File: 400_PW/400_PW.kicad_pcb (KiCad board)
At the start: 2 copper layers, 97.4 x 67.5 mm, 0 parts

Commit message: Update schematics
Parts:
- added C1: C_0038, DVB_Capacitors_Ceramic:C_1206, F.Cu at (131.7, 262.0)
- added C10: C_0032, DVB_Capacitors_Ceramic:C_0805, F.Cu at (147.6, 250.1)
- added C11: C_0002, DVB_Capacitors_Ceramic:C_0402, F.Cu at (102.6, 268.9)
- added C12: C_0002, DVB_Capacitors_Ceramic:C_0402, F.Cu at (121.7, 263.1)
- added C13: C_0002, DVB_Capacitors_Ceramic:C_0402, F.Cu at (141.5, 258.9)
- added C14: C_0038, DVB_Capacitors_Ceramic:C_1206, F.Cu at (142.1, 246.2)
- added C15: C_0037, DVB_Capacitors_Ceramic:C_0603, F.Cu at (157.9, 241.4)
- added C16: C_0037, DVB_Capacitors_Ceramic:C_0603, F.Cu at (152.4, 246.1)
- added C17: C_0037, DVB_Capacitors_Ceramic:C_0603, F.Cu at (141.9, 256.7)
- added C18: C_0032, DVB_Capacitors_Ceramic:C_0805, F.Cu at (136.8, 261.8)
- added C19: C_0071, DVB_Capacitors_Ceramic:C_2220, F.Cu at (117.6, 254.3)
- added C2: C_0038, DVB_Capacitors_Ceramic:C_1206, F.Cu at (131.6, 253.7)
- added C20: C_0012, DVB_Capacitors_Ceramic:C_0603, F.Cu at (110.6, 235.3)
- added C21: C_0012, DVB_Capacitors_Ceramic:C_0603, F.Cu at (157.9, 239.1)
- added C22: C_0012, DVB_Capacitors_Ceramic:C_0603, F.Cu at (118.0, 241.3)
- added C23: C_0071, DVB_Capacitors_Ceramic:C_2220, F.Cu at (139.0, 231.4)
- added C24: C_0039, DVB_Capacitors_Ceramic:C_0402, F.Cu at (114.1, 235.1)
- added C25: C_0039, DVB_Capacitors_Ceramic:C_0402, F.Cu at (140.6, 261.4)
- added C26: C_0039, DVB_Capacitors_Ceramic:C_0402, F.Cu at (102.6, 266.9)
- added C27: C_0040, DVB_Capacitors_Ceramic:C_1210, F.Cu at (149.9, 236.9)
- added C28: C_0040, DVB_Capacitors_Ceramic:C_1210, F.Cu at (131.6, 257.3)
- added C29: C_0040, DVB_Capacitors_Ceramic:C_1210, F.Cu at (147.7, 242.5)
- added C3: C_0038, DVB_Capacitors_Ceramic:C_1206, F.Cu at (98.3, 267.4)
- added C30: C_0071, DVB_Capacitors_Ceramic:C_2220, F.Cu at (108.9, 261.1)
- added C31: C_0040, DVB_Capacitors_Ceramic:C_1210, F.Cu at (155.4, 235.9)
- added C32: C_0040, DVB_Capacitors_Ceramic:C_1210, F.Cu at (126.2, 264.1)
- added C33: C_0040, DVB_Capacitors_Ceramic:C_1210, F.Cu at (137.2, 254.3)
- added C34: C_0040, DVB_Capacitors_Ceramic:C_1210, F.Cu at (147.7, 246.6)
- added C35: C_0040, DVB_Capacitors_Ceramic:C_1210, F.Cu at (126.2, 268.2)
- added C36: C_0040, DVB_Capacitors_Ceramic:C_1210, F.Cu at (163.1, 258.9)
- added C37: C_0040, DVB_Capacitors_Ceramic:C_1210, F.Cu at (137.2, 258.4)
- added C38: C_0040, DVB_Capacitors_Ceramic:C_1210, F.Cu at (138.0, 250.2)
- added C39: C_0040, DVB_Capacitors_Ceramic:C_1210, F.Cu at (120.6, 266.6)
- added C4: C_0002, DVB_Capacitors_Ceramic:C_0402, F.Cu at (127.2, 259.9)
- added C40: C_0037, DVB_Capacitors_Ceramic:C_0603, F.Cu at (163.6, 264.5)
- added C41: C_0057, DVB_Capacitors_Ceramic:C_0603, F.Cu at (163.6, 262.2)
- added C42: C_0041, DVB_Capacitors_Ceramic:C_1206, F.Cu at (153.2, 240.5)
- added C43: C_0056, DVB_Capacitors_Ceramic:C_0805, F.Cu at (131.2, 265.0)
- added C44: C_0003, DVB_Capacitors_Ceramic:C_0603, F.Cu at (121.8, 241.3)
- added C45: C_0058, DVB_Capacitors_Tantalum:CP_EIA-7343-31, F.Cu at (92.7, 237.0)
- added C5: C_0038, DVB_Capacitors_Ceramic:C_1206, F.Cu at (132.5, 249.8)
- added C6: C_0038, DVB_Capacitors_Ceramic:C_1206, F.Cu at (142.1, 243.0)
- added C7: C_0038, DVB_Capacitors_Ceramic:C_1206, F.Cu at (122.9, 260.5)
- added C8: C_0032, DVB_Capacitors_Ceramic:C_0805, F.Cu at (152.7, 243.5)
- added C9: C_0032, DVB_Capacitors_Ceramic:C_0805, F.Cu at (143.1, 250.1)
- added D1: D_0026, DVB_Diodes:D_SMA, F.Cu at (109.4, 251.0)
- added D2: D_0026, DVB_Diodes:D_SMA, F.Cu at (130.8, 230.4)
- added D3: D_0026, DVB_Diodes:D_SMA, F.Cu at (129.2, 236.4)
- added D4: D_0026, DVB_Diodes:D_SMA, F.Cu at (100.4, 263.6)
- added D5: D_0026, DVB_Diodes:D_SMA, F.Cu at (91.4, 266.3)
- added D6: D_0026, DVB_Diodes:D_SMA, F.Cu at (109.4, 255.6)
- added J1: TESTBAT-14, DVB_Connectors:Solder_Pad_8x5, B.Cu at (203.7, 207.8)
- added J10: GNDBATT-4B, DVB_Connectors:Solder_Pad_8x5, B.Cu at (203.1, 187.9)
- added J11: GND-7_21_22_3B_28_51B_53_76, DVB_Connectors:Solder_Pad_8x5, B.Cu at (204.1, 227.0)
- added J12: TESTBAT-14, DVB_Connectors:Solder_Pad_8x5, B.Cu at (203.9, 238.7)
- added J2: ON/OFF-6A, DVB_Connectors:Solder_Pad_8x5, B.Cu at (137.7, 169.4)
- added J3: +7.5V-13_26_33_51A_54_104_6A, DVB_Connectors:Solder_Pad_8x5, B.Cu at (203.5, 249.1)
- added J4: +4.9V-10_36_80_83_93, DVB_Connectors:Solder_Pad_8x5, B.Cu at (152.1, 171.5)
- added J5: -4.9V, DVB_Connectors:Solder_Pad_8x5, B.Cu at (203.4, 198.0)
- added J6: +48V, DVB_Connectors:Solder_Pad_8x5, B.Cu at (195.4, 176.2)
- added J7: BATT-4A_6B, DVB_Connectors:Solder_Pad_8x5, B.Cu at (204.0, 218.9)
- added J8: 15VIN-3A, DVB_Connectors:Solder_Pad_8x5, B.Cu at (200.3, 268.6)
- added J9: GNDAKKU-5, DVB_Connectors:Solder_Pad_8x5, B.Cu at (178.9, 171.3)
- added K1: K_0008, Connector_JST:JST_EH_B3B-EH-A_1x03_P2.50mm_Vertical, B.Cu at (87.1, 186.7)
- added L1: L_0001, DVB_Inductors:L_0805, F.Cu at (130.8, 267.8)
- added L10: L_0004, DVB_Inductors:L_2020-Vishay, F.Cu at (116.6, 261.2)
- added L11: L_0001, DVB_Inductors:L_0805, F.Cu at (151.8, 250.1)
- added L12: L_0004, DVB_Inductors:L_2020-Vishay, F.Cu at (136.9, 238.0)
- added L2: L_0001, DVB_Inductors:L_0805, F.Cu at (147.2, 252.9)
- added L3: L_0001, DVB_Inductors:L_0805, F.Cu at (135.4, 265.0)
- added L4: L_0004, DVB_Inductors:L_2020-Vishay, F.Cu at (146.7, 231.5)
- added L5: L_0004, DVB_Inductors:L_2020-Vishay, F.Cu at (135.8, 244.8)
- added L6: L_0004, DVB_Inductors:L_2020-Vishay, F.Cu at (125.3, 255.5)
- added L7: L_0015, DVB_Inductors:L_7050-Wurth, F.Cu at (104.0, 232.4)
- added L8: L_0004, DVB_Inductors:L_2020-Vishay, F.Cu at (126.1, 248.8)
- added L9: L_0004, DVB_Inductors:L_2020-Vishay, F.Cu at (128.6, 242.0)
- added R1: R_0002, DVB_Resistors:R_0402, F.Cu at (155.6, 246.0)
- added R10: R_0002, DVB_Resistors:R_0402, F.Cu at (143.4, 261.1)
- added R11: R_0155, DVB_Resistors:R_0402, F.Cu at (158.3, 245.9)
- added R12: R_0002, DVB_Resistors:R_0402, F.Cu at (147.8, 255.4)
- added R13: R_0158, DVB_Resistors:R_0402, F.Cu at (164.6, 269.0)
- added R14: R_0002, DVB_Resistors:R_0402, F.Cu at (144.3, 258.9)
- added R15: R_0008, DVB_Resistors:R_0402, F.Cu at (145.1, 256.6)
- added R16: R_0112, DVB_Resistors:R_0402, F.Cu at (155.6, 248.2)
- added R17: R_0128, DVB_Resistors:R_0402, F.Cu at (150.4, 252.6)
- added R18: R_0099, DVB_Resistors:R_1206, F.Cu at (142.6, 253.9)
- added R19: R_0157, DVB_Resistors:R_0402, F.Cu at (138.6, 264.3)
- added R2: R_0159, DVB_Resistors:R_0402, F.Cu at (156.3, 243.7)
- added R20: R_0034, DVB_Resistors:R_0402, F.Cu at (159.0, 243.7)
- added R21: R_0020, DVB_Resistors:R_0402, F.Cu at (134.0, 267.5)
- added R3: R_0156, DVB_Resistors:R_0402, F.Cu at (164.6, 266.8)
- added R4: R_0156, DVB_Resistors:R_0402, F.Cu at (136.7, 267.5)
- added R5: R_0156, DVB_Resistors:R_0402, F.Cu at (150.4, 254.8)
- added R6: R_0154, DVB_Resistors:R_0402, F.Cu at (155.0, 250.3)
- added R7: R_0118, DVB_Resistors:R_0402, F.Cu at (153.0, 252.6)
- added R8: R_0002, DVB_Resistors:R_0402, F.Cu at (147.8, 257.6)
- added R9: R_0155, DVB_Resistors:R_0402, F.Cu at (141.2, 263.6)
- added RV1: 25K, Potentiometer_THT:Potentiometer_Piher_PT-6-V_Vertical_Hole, F.Cu at (174.6, 246.6)
- added U1: U_0064, DVB_SSOP:MSOP_16-1EP_3x4_P0.5, F.Cu at (114.5, 267.5)
- added U2: U_0064, DVB_SSOP:MSOP_16-1EP_3x4_P0.5, F.Cu at (107.9, 267.3)
- added U3: U_0064, DVB_SSOP:MSOP_16-1EP_3x4_P0.5, F.Cu at (153.6, 231.0)
- added U4: U_0126, DVB_SOIC:SOIC_8, F.Cu at (100.6, 258.0)
- added U5: U_0089, DVB_SSOP:MSOP_12-1EP_3x4_P0.65, F.Cu at (143.8, 237.7)
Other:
- outline, holes or cut-outs redrawn

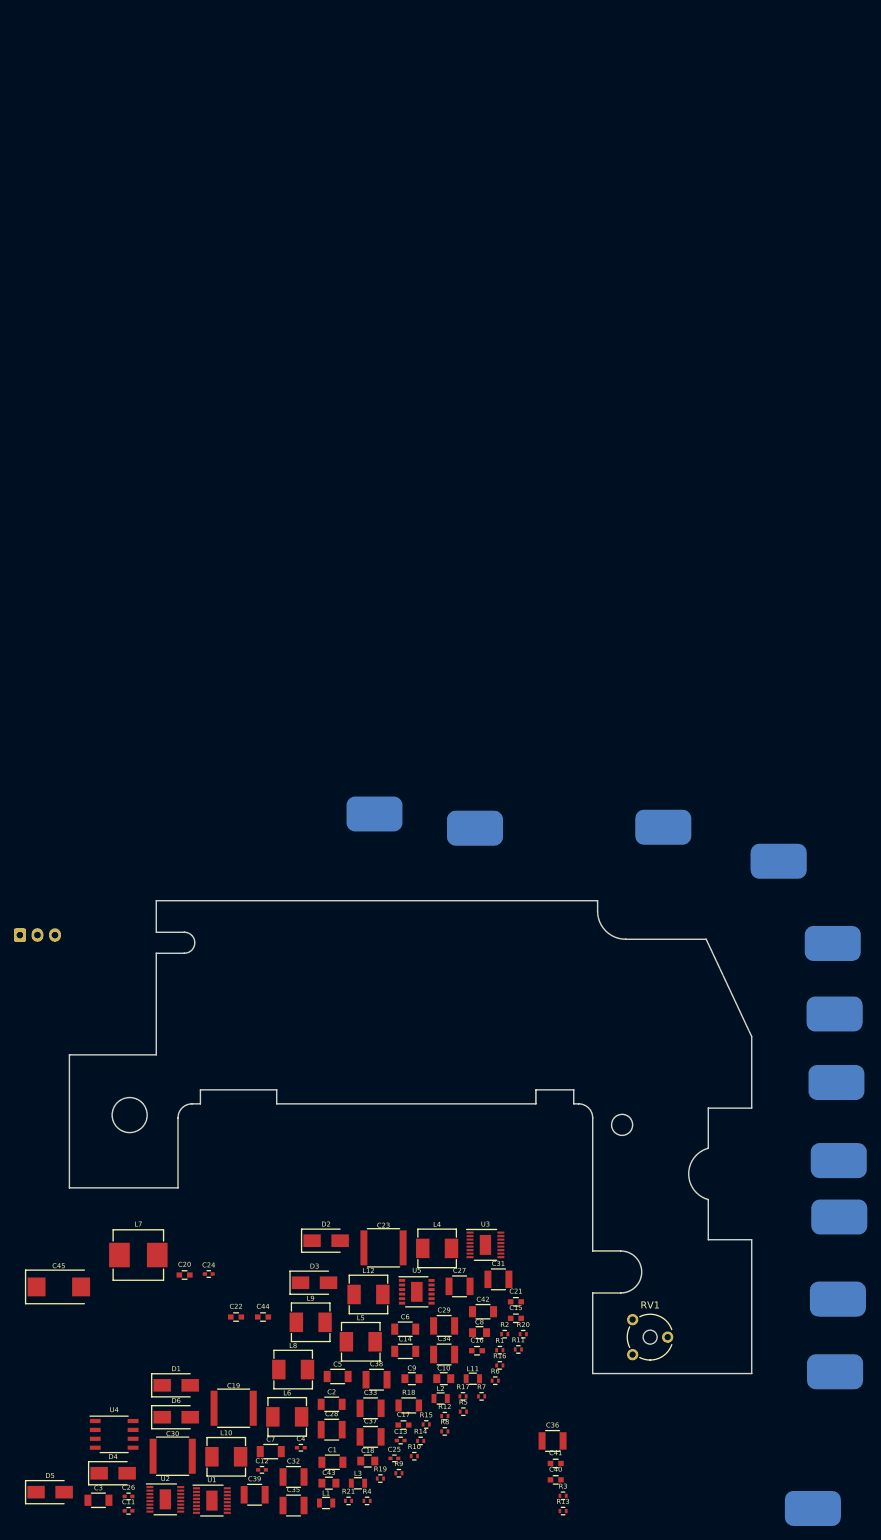
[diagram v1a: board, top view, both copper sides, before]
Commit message: Place components on 400_PW
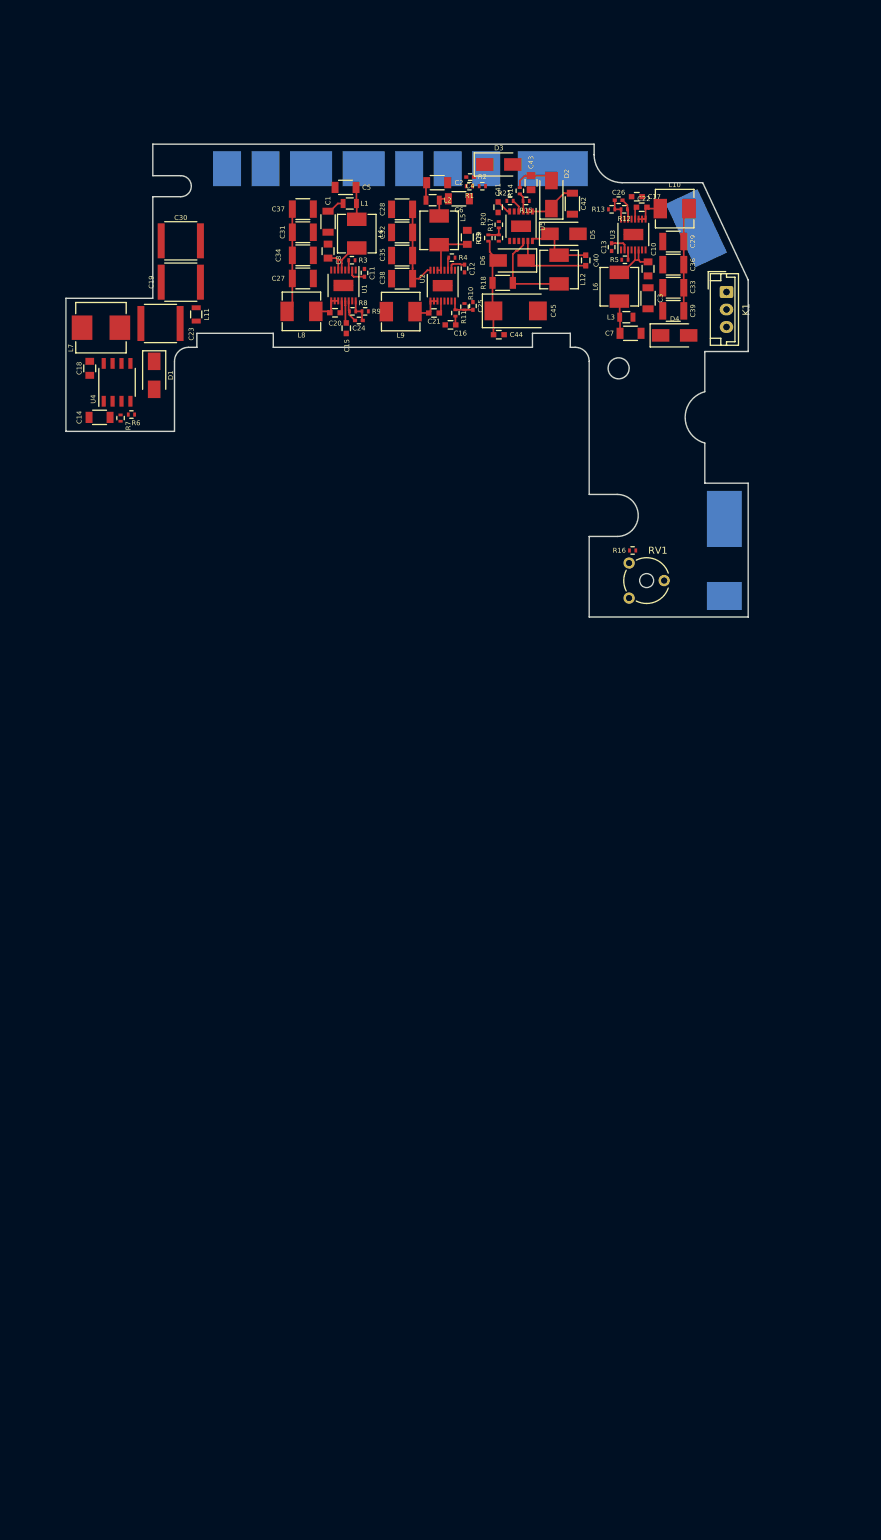
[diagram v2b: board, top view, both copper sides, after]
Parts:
- removed J10: GNDBATT-4B, DVB_Connectors:Solder_Pad_8x5
- removed J9: GNDAKKU-5, DVB_Connectors:Solder_Pad_8x5
- added J13: GND, DVB_Connectors:Solder_Pad_8x5, B.Cu at (187.7, 127.3)
- J7: value BATT-4A_6B -> ON/OFF-4A_6B
- K1: moved to F.Cu
- moved C26 197.8 mm to (172.6, 81.8), turned to 180 degrees
- moved J8 196.9 mm to (153.7, 77.3)
- moved D5 194.0 mm to (164.8, 86.6)
- moved L10 189.3 mm to (180.6, 83.0)
- moved C3 188.7 mm to (176.8, 95.8), turned to 270 degrees
- moved C43 187.9 mm to (160.1, 79.3), turned to 90 degrees
- moved R21 187.0 mm to (157.1, 81.9), turned to 180 degrees
- moved R13 186.0 mm to (171.6, 83.1)
- moved L1 185.5 mm to (134.2, 82.3)
- moved C4 183.0 mm to (151.4, 78.5), turned to 180 degrees
- moved D4 181.1 mm to (180.6, 101.1)
- moved J12 180.9 mm to (122.2, 77.3)
- moved C11 179.9 mm to (136.3, 92.2), turned to 90 degrees
- moved C41 179.5 mm to (155.4, 82.8), turned to 270 degrees
- moved C39 179.3 mm to (180.4, 97.6), turned to 180 degrees
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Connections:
- C40 pad 1: GND -> Net-(C40-Pad1)
- C40 pad 2: +15 -> Net-(C40-Pad2)
- C43 pad 1: Net-(C43-Pad1) -> GND
- C43 pad 2: Net-(C43-Pad2) -> +15
- D5 pad 1: Net-(C43-Pad1) -> Net-(C40-Pad1)
- D6 pad 1: Net-(C43-Pad2) -> Net-(C40-Pad2)
- J7 pad 1: +BATT -> VDD
- L12 pad 1: Net-(C43-Pad1) -> Net-(C40-Pad1)
- U5 pad 11: Net-(C43-Pad2) -> Net-(C40-Pad2)
- U5 pad 12: Net-(C43-Pad1) -> Net-(C40-Pad1)
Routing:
- net +4.9V: track 0.00 -> 18.1 mm
- net +7.5V: track 0.00 -> 17.9 mm
- net +BATT: track 0.00 -> 14.2 mm
- net -4.9V: track 0.00 -> 14.2 mm
- net Net-(L12-Pad2): track 0.00 -> 13.4 mm
- net Net-(C40-Pad2): track 0.00 -> 11.7 mm
- net Net-(C40-Pad1): track 0.00 -> 10.5 mm
- net Net-(C9-Pad1): track 0.00 -> 8.64 mm
- net Net-(C10-Pad1): track 0.00 -> 7.83 mm
- net Net-(C8-Pad1): track 0.00 -> 7.78 mm
- net Net-(C42-Pad1): track 0.00 -> 7.67 mm
- net Net-(C20-Pad2): track 0.00 -> 6.69 mm
- net +15: track 0.00 -> 6.07 mm
- net VDD: track 0.00 -> 5.15 mm
- net Net-(C21-Pad2): track 0.00 -> 4.84 mm
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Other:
- outline, holes or cut-outs redrawn

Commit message: Update PW 400
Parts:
- added C46: C_0002, DVB_Capacitors_Ceramic:C_0402, F.Cu at (97.5, 108.4)
- added G***: LOGO, DVB_Mechanicals:LogoUher2, B.Cu at (99.1, 97.9)
- added G***: LOGO, LogoUher1, B.Cu at (124.4, 95.0)
- added J9: ON/OFF-48V, DVB_Connectors:Solder_Pad_8x5, B.Cu at (122.9, 77.3)
- added R22: R_0034, DVB_Resistors:R_0402, F.Cu at (97.5, 110.5)
- added REF**: MountingHole_3.2mm_M3_Pad_Via, MountingHole:MountingHole_3.2mm_M3_Pad_Via, F.Cu at (172.6, 105.8)
- added REF1: CircleWhite1mm, DVB_Fiducials:REF_1mm, F.Cu at (107.8, 75.5)
- added REF1: MountingHole_3.2mm_M3_Pad_Via, MountingHole:MountingHole_3.2mm_M3_Pad_Via, F.Cu at (110.1, 79.8)
- added REF2: CircleWhite1mm, DVB_Fiducials:REF_1mm, F.Cu at (189.4, 101.7)
- added REF3: CircleWhite1mm, DVB_Fiducials:REF_1mm, F.Cu at (189.4, 134.0)
- K1: value K_0008 -> BATT; footprint Connector_JST:JST_EH_B3B-EH-A_1x03_P2.50mm_Vertical -> Connector_JST:JST_VH_B2P-VH_1x02_P3.96mm_Vertical; moved to B.Cu
- RV1: footprint Potentiometer_THT:Potentiometer_Piher_PT-6-V_Vertical_Hole -> Potentiometer_THT:Potentiometer_Piher_PT-10-V10_Vertical_Hole
- moved C43 13.7 mm to (168.1, 90.4), turned to 270 degrees
- moved C40 12.4 mm to (165.6, 78.2)
- moved R16 10.8 mm to (184.0, 137.1)
- moved L11 9.11 mm to (112.8, 89.0), turned to 0 degrees
- moved RV1 9.11 mm to (181.6, 133.5), turned to 180 degrees
- moved C30 8.82 mm to (117.5, 92.4), turned to 90 degrees
- moved J12 5.10 mm to (127.3, 77.3)
- moved C7 5.01 mm to (169.8, 98.6), turned to 180 degrees
- moved J4 4.50 mm to (133.2, 77.3)
- moved J5 4.40 mm to (140.6, 77.3)
- moved D4 4.20 mm to (182.8, 104.7), turned to 90 degrees
- moved C5 3.82 mm to (137.3, 80.8), turned to 90 degrees
- moved J7 3.80 mm to (146.5, 77.3)
- moved K1 2.71 mm to (185.4, 95.7)
- moved J2 2.70 mm to (150.9, 77.3)
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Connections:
- C40 pad 1: Net-(C40-Pad1) -> GND
- C40 pad 2: Net-(C40-Pad2) -> +15
- C43 pad 1: GND -> Net-(C43-Pad1)
- C43 pad 2: +15 -> Net-(C43-Pad2)
- D5 pad 1: Net-(C40-Pad1) -> Net-(C43-Pad1)
- D6 pad 1: Net-(C40-Pad2) -> Net-(C43-Pad2)
- K1 pad 2: /NTC -> +BATT
- L12 pad 1: Net-(C40-Pad1) -> Net-(C43-Pad1)
- U4 pad 1: +7.5V -> /EN_48V
- U5 pad 11: Net-(C40-Pad2) -> Net-(C43-Pad2)
- U5 pad 12: Net-(C40-Pad1) -> Net-(C43-Pad1)
- U5 pad 8: /NTC -> (no net)
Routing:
- net GND: track 0.00 -> 330.0 mm, vias 0 -> 75
- net VDD: track 5.15 -> 173.8 mm, vias 0 -> 18
- net /PW_EN: track 0.00 -> 84.5 mm, vias 0 -> 1
- net +7.5V: track 17.9 -> 83.5 mm, vias 0 -> 6
- net +BATT: track 14.2 -> 66.0 mm, vias 0 -> 3
- net /EN_48V: track 0.00 -> 48.9 mm, vias 0 -> 1
- net -4.9V: track 14.2 -> 54.9 mm, vias 0 -> 12
- net /CHG_LED: track 0.00 -> 35.6 mm, vias 0 -> 1
- net +48V: track 0.00 -> 33.3 mm, vias 0 -> 3
- net Net-(R1-Pad1): track 0.00 -> 29.5 mm, vias 0 -> 2
- net +4.9V: track 18.1 -> 37.4 mm, vias 0 -> 5
- net Net-(C19-Pad2): track 0.00 -> 14.3 mm, vias 0 -> 2
- net Net-(C40-Pad2): track 11.7 -> 0.00 mm
- net Net-(C40-Pad1): track 10.5 -> 0.00 mm
- net +15: track 6.07 -> 13.4 mm, vias 0 -> 2
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- added copper zone on F.Cu, net +15
- added copper zone on B.Cu, net +4.9V
- added copper zone on F.Cu, net +4.9V
- added copper zone on F.Cu, net +48V
- added copper zone on F.Cu, net +7.5V
- added copper zone on F.Cu, net +BATT
- added copper zone on B.Cu, net -4.9V
- added copper zone on F.Cu, net -4.9V
- added copper zone on B.Cu, net GND
- added copper zone on F.Cu, net GND
- added copper zone on GND.Cu, net GND
- added copper zone on F.Cu, net Net-(C10-Pad1)
- added copper zone on F.Cu, net Net-(C19-Pad2)
- added copper zone on F.Cu, net Net-(C20-Pad2)
- added copper zone on F.Cu, net Net-(C21-Pad2)
- added copper zone on F.Cu, net Net-(C22-Pad2)
- added copper zone on F.Cu, net Net-(C42-Pad1)
- added copper zone on F.Cu, net Net-(C43-Pad1)
- added copper zone on F.Cu, net Net-(C43-Pad2)
- added copper zone on F.Cu, net Net-(C5-Pad1)
- added copper zone on F.Cu, net Net-(C6-Pad1)
- added copper zone on F.Cu, net Net-(C7-Pad1)
- added copper zone on F.Cu, net Net-(C8-Pad1)
- added copper zone on F.Cu, net Net-(C9-Pad1)
- added copper zone on F.Cu, net Net-(D1-Pad2)
- added copper zone on F.Cu, net Net-(L12-Pad2)
- added copper zone on F.Cu, net VDD
- added copper zone on POWER.Cu, net VDD
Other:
- outline, holes or cut-outs redrawn
- copper layers 2 -> 4
- board text added: "+"
- board text added: "+15V"
- board text added: "+4.9V"
- board text added: "+48V"
- board text added: "+7.5V"
- board text added: "-"
- board text added: "-4.9V"
- board text added: "CHG-LED"
- board text added: "EN"
- board text added: "EN48"
- board text added: "GND"
- board text added: "POWER -400- v1.0.0 PLF 2019"
- board text added: "VDD"
- board text added: "VU"
- board text added: "Verifier : - La masse au GND - L'écartement des vis ainsi que le diamètre - Le passage des composants sous le PCB - Les propriètés du cnnecteur batterie - Simuler le comportement du vu-mètre"
